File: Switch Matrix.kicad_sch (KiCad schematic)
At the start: 136 parts, among them SW1 RotaryEncoder_Switch, SW10 SW_Push_45deg, SW11 SW_Push_45deg, SW11(2)1 SW_Push_45deg, SW12 SW_Push_45deg, SW13 SW_Push_45deg, SW14 SW_Push_45deg, SW15 SW_Push_45deg, SW16 SW_Push_45deg, SW17 SW_Push_45deg, SW18 SW_Push_45deg, SW19 SW_Push_45deg, SW2 SW_Push_45deg, SW20 SW_Push_45deg, SW21 SW_Push_45deg, SW22 SW_Push_45deg, SW22(1.5)1 SW_Push_45deg, SW23 SW_Push_45deg, SW23(1.5)1 SW_Push_45deg, SW24 SW_Push_45deg, SW24(2)1 SW_Push_45deg, SW24(ISO)1 SW_Push_45deg, SW25(1.25)1 SW_Push_45deg, SW25(1.5)1 SW_Push_45deg, SW25(ortho)1 SW_Push_45deg, SW26 SW_Push_45deg, SW26(ortho)1 SW_Push_45deg, SW27 SW_Push_45deg, SW27(ortho)1 SW_Push_45deg, SW28 SW_Push_45deg, SW28(ortho)1 SW_Push_45deg, SW29 SW_Push_45deg, SW29(ortho)1 SW_Push_45deg, SW3 SW_Push_45deg, SW30 SW_Push_45deg, SW30(ortho)1 SW_Push_45deg, SW31 SW_Push_45deg, SW31(ortho)1 SW_Push_45deg, SW32 SW_Push_45deg, SW32(ortho)1 SW_Push_45deg, SW33 SW_Push_45deg, SW33(ortho)1 SW_Push_45deg, SW34 SW_Push_45deg, SW34(ortho)1 SW_Push_45deg, SW35 SW_Push_45deg, SW35(ortho)1 SW_Push_45deg, SW36(1.25)1 SW_Push_45deg, SW36(1.5)1 SW_Push_45deg, SW36(ortho)1 SW_Push_45deg, SW37 SW_Push_45deg, SW37(1.5)1 SW_Push_45deg, SW38 SW_Push_45deg, SW38(3)1 SW_Push_45deg, SW39 SW_Push_45deg, SW39(1.5)1 SW_Push_45deg, SW4 SW_Push_45deg, SW40(1.25)1 SW_Push_45deg, SW40(1.5)1 SW_Push_45deg, SW40(3)1 SW_Push_45deg, SW41 SW_Push_45deg, SW41(1.75)1 SW_Push_45deg, SW41(1.75a)1 SW_Push_45deg, SW41(1.75a)2 SW_Push_45deg, SW41(2)1 SW_Push_45deg, SW41(2.25)1 SW_Push_45deg, SW42 SW_Push_45deg, SW42(3)1 SW_Push_45deg, SW42(6)1 SW_Push_45deg, SW43 SW_Push_45deg, SW43(1.75)1 SW_Push_45deg, SW43(2)1 SW_Push_45deg, SW43(2.25)1 SW_Push_45deg, SW44 SW_Push_45deg, SW44(1.25)1 SW_Push_45deg, SW44(1.5)1 SW_Push_45deg, SW44(3)1 SW_Push_45deg, SW45 SW_Push_45deg, SW45(1.5)1 SW_Push_45deg, SW46 SW_Push_45deg, SW46(3)1 SW_Push_45deg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

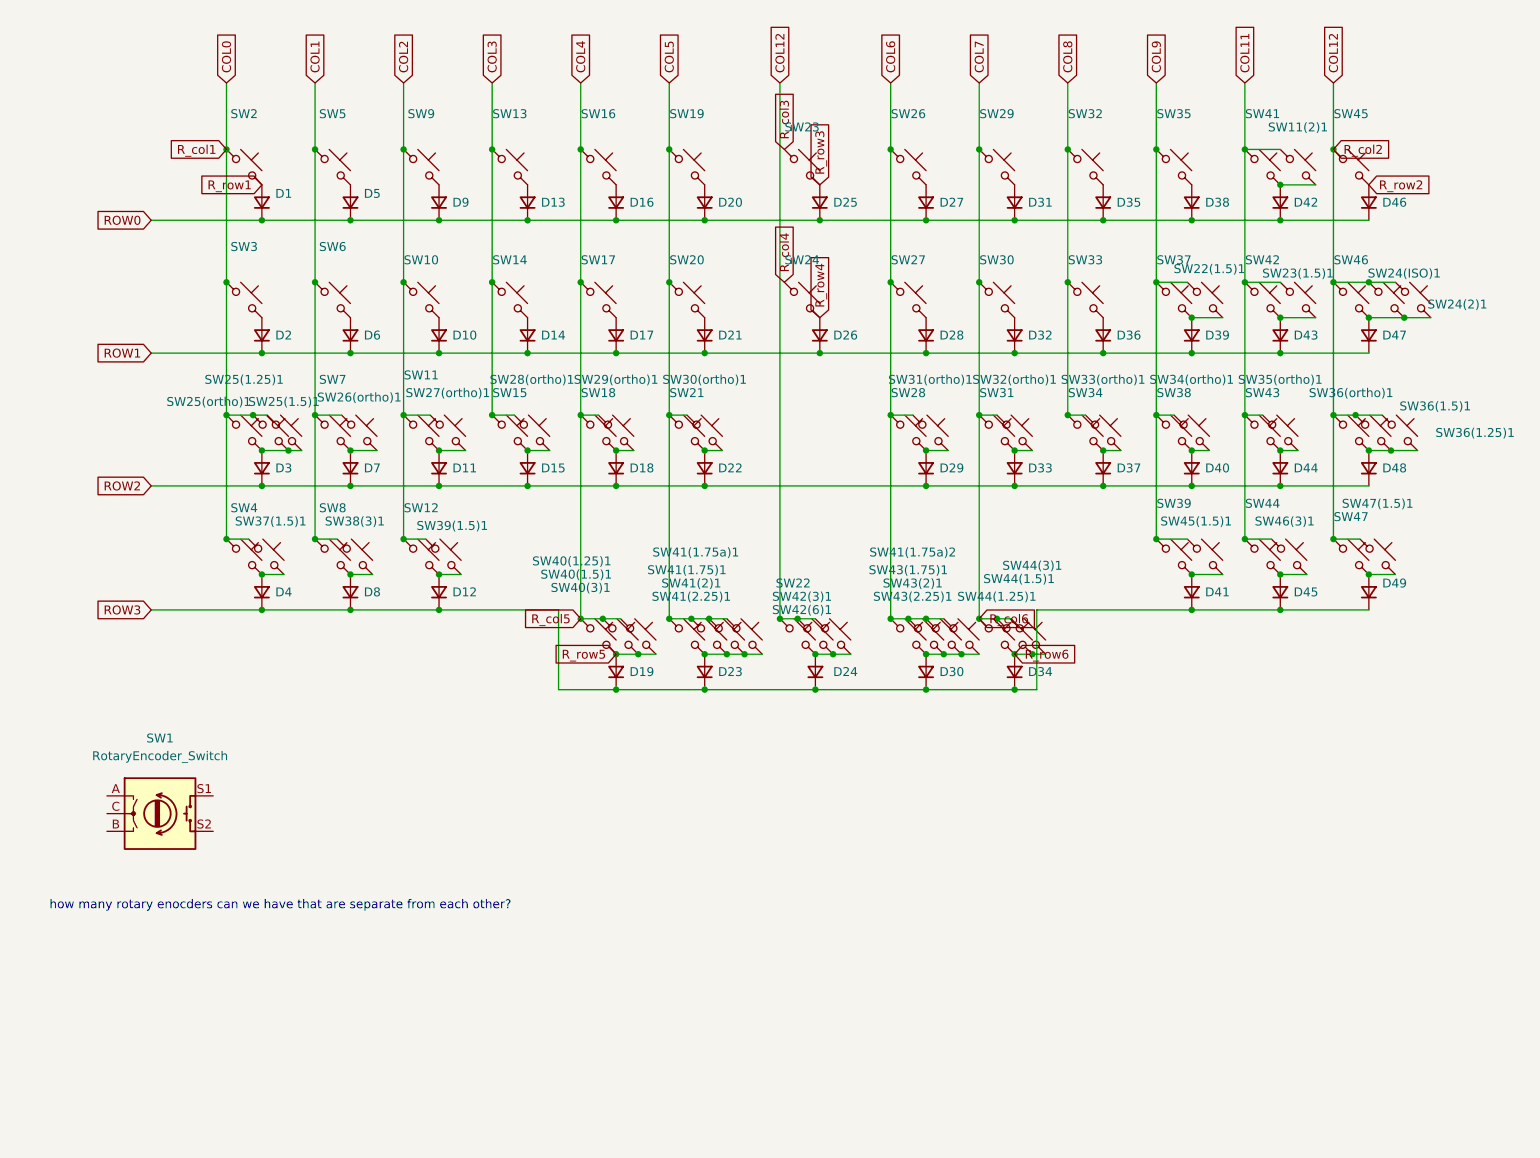
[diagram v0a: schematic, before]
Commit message: edited schematics, assigned footprints
4u spacebar missing, no appropriate footprint in library yet
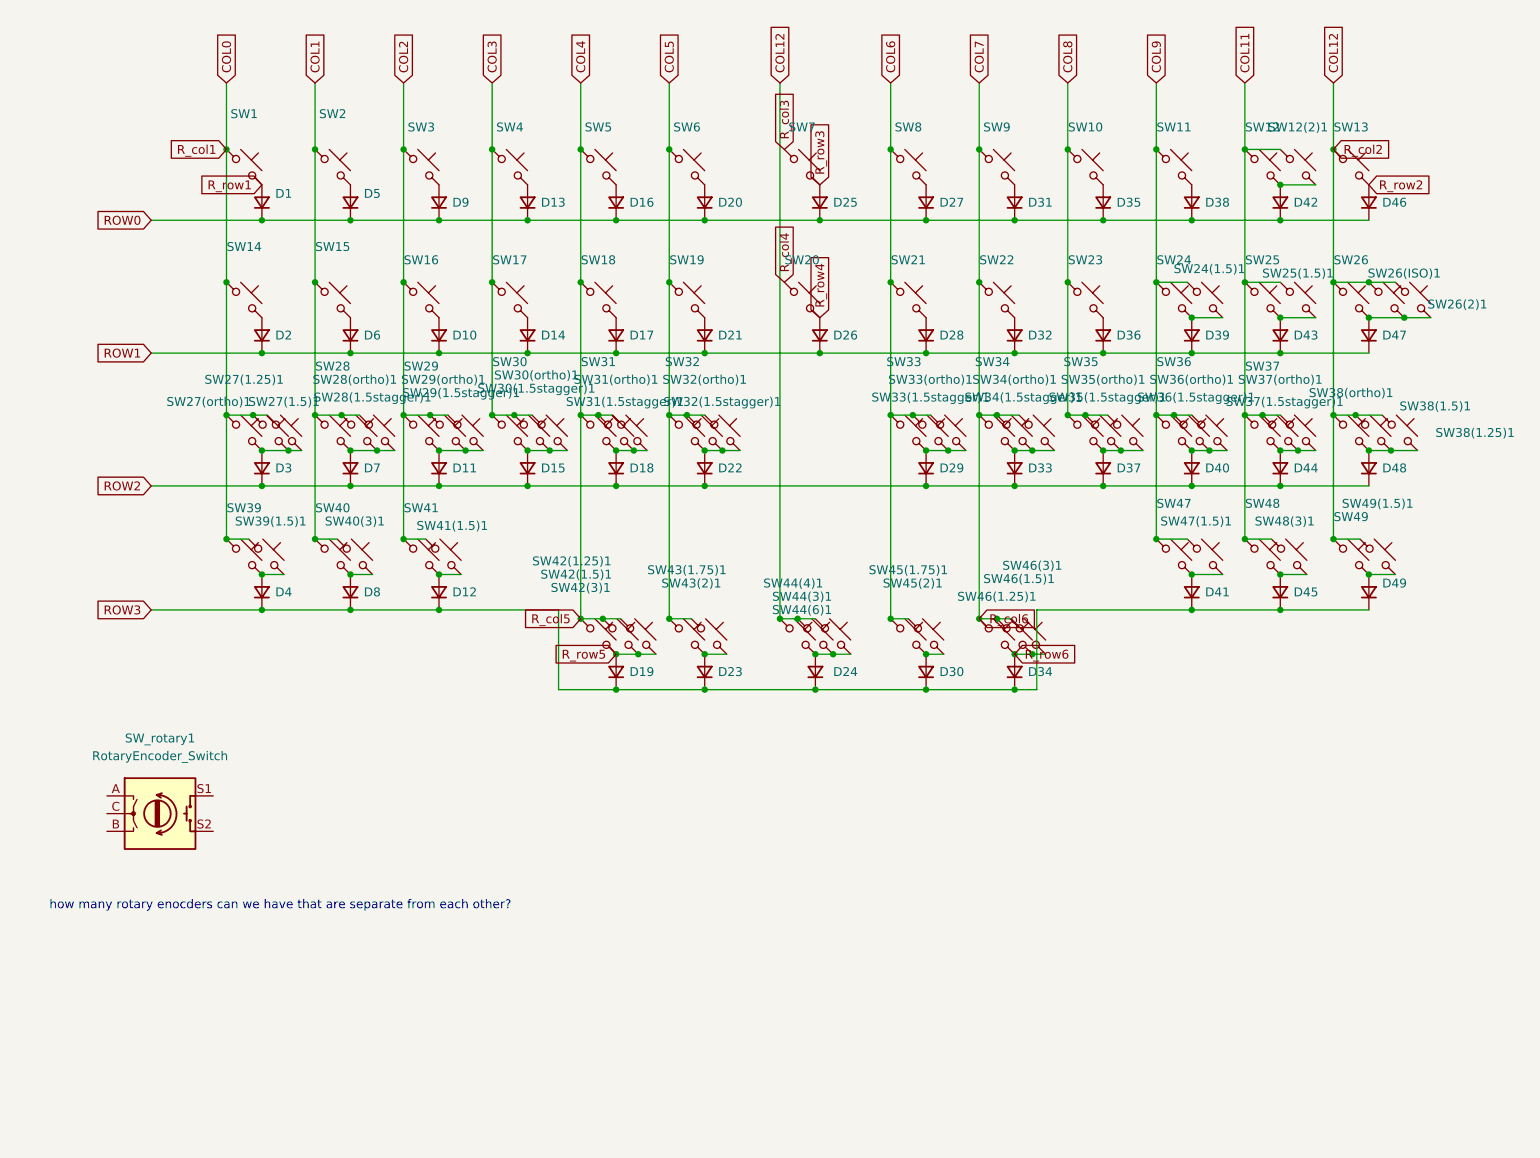
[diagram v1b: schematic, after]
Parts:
- removed SW41(1.75a)1, SW41(1.75a)2, SW41(2.25)1, SW43(2.25)1: SW_Push_45deg, symbol Switch:SW_Push_45deg
- added SW28(1.5stagger)1, SW29(1.5stagger)1, SW30(1.5stagger)1, SW31(1.5stagger)1, SW32(1.5stagger)1, SW33(1.5stagger)1, SW34(1.5stagger)1, SW35(1.5stagger)1, SW36(1.5stagger)1, SW37(1.5stagger)1: SW_Push_45deg, MX_Only:MXOnly-1U-NoLED, symbol Switch:SW_Push_45deg
- D1, D10, D11, D12, D13, D14, D15, D16, D17, D18, D19, D2, D20, D21, D22, D23, D24, D25, D26, D27, D28, D29, D3, D30, D31, D32, D33, D34, D35, D36, D37, D38, D39, D4, D40, D41, D42, D43, D44, D45, D46, D47, D48, D49, D5, D6, D7, D8, D9: footprint (none) -> Diode_SMD:D_SOD-123F
- SW1: renamed from SW2; footprint (none) -> MX_Only:MXOnly-1U-NoLED
- SW10: renamed from SW32; footprint (none) -> MX_Only:MXOnly-1U-NoLED
- SW11: renamed from SW35; footprint (none) -> MX_Only:MXOnly-1U-NoLED
- SW12: renamed from SW41; footprint (none) -> MX_Only:MXOnly-1U-NoLED
- SW12(2)1: renamed from SW11(2)1; footprint (none) -> MX_Only:MXOnly-2U-NoLED
- SW13: renamed from SW45; footprint (none) -> MX_Only:MXOnly-1U-NoLED
- SW14: renamed from SW3; footprint (none) -> MX_Only:MXOnly-1U-NoLED
- SW15: renamed from SW6; footprint (none) -> MX_Only:MXOnly-1U-NoLED
- SW16: renamed from SW10; footprint (none) -> MX_Only:MXOnly-1U-NoLED
- SW17: renamed from SW14; footprint (none) -> MX_Only:MXOnly-1U-NoLED
- SW18: renamed from SW17; footprint (none) -> MX_Only:MXOnly-1U-NoLED
- SW19: renamed from SW20; footprint (none) -> MX_Only:MXOnly-1U-NoLED
- SW2: renamed from SW5; footprint (none) -> MX_Only:MXOnly-1U-NoLED
- SW20: renamed from SW24; footprint (none) -> MX_Only:MXOnly-1U-NoLED
- SW21: renamed from SW27; footprint (none) -> MX_Only:MXOnly-1U-NoLED
- SW22: renamed from SW30; footprint (none) -> MX_Only:MXOnly-1U-NoLED
- SW23: renamed from SW33; footprint (none) -> MX_Only:MXOnly-1U-NoLED
- SW24: renamed from SW37; footprint (none) -> MX_Only:MXOnly-1U-NoLED
- SW24(1.5)1: renamed from SW22(1.5)1; footprint (none) -> MX_Only:MXOnly-1.5U-NoLED
- SW25: renamed from SW42; footprint (none) -> MX_Only:MXOnly-1U-NoLED
- SW25(1.5)1: renamed from SW23(1.5)1; footprint (none) -> MX_Only:MXOnly-1.5U-NoLED
- SW26: renamed from SW46; footprint (none) -> MX_Only:MXOnly-1U-NoLED
- SW26(2)1: renamed from SW24(2)1; footprint (none) -> MX_Only:MXOnly-2U-NoLED
- SW26(ISO)1: renamed from SW24(ISO)1; footprint (none) -> MX_Only:MXOnly-ISO-NoLED
- SW27(1.25)1: renamed from SW25(1.25)1; footprint (none) -> MX_Only:MXOnly-1.25U-NoLED
- SW27(1.5)1: renamed from SW25(1.5)1; footprint (none) -> MX_Only:MXOnly-1.5U-NoLED
- SW27(ortho)1: renamed from SW25(ortho)1; footprint (none) -> MX_Only:MXOnly-1U-NoLED
- SW28: renamed from SW7; footprint (none) -> MX_Only:MXOnly-1U-NoLED
- SW28(ortho)1: renamed from SW26(ortho)1; footprint (none) -> MX_Only:MXOnly-1U-NoLED
- SW29: renamed from SW11; footprint (none) -> MX_Only:MXOnly-1U-NoLED
- SW29(ortho)1: renamed from SW27(ortho)1; footprint (none) -> MX_Only:MXOnly-1U-NoLED
- SW3: renamed from SW9; footprint (none) -> MX_Only:MXOnly-1U-NoLED
- SW30: renamed from SW15; footprint (none) -> MX_Only:MXOnly-1U-NoLED
- SW30(ortho)1: renamed from SW28(ortho)1; footprint (none) -> MX_Only:MXOnly-1U-NoLED
- SW31: renamed from SW18; footprint (none) -> MX_Only:MXOnly-1U-NoLED
- SW31(ortho)1: renamed from SW29(ortho)1; footprint (none) -> MX_Only:MXOnly-1U-NoLED
- SW32: renamed from SW21; footprint (none) -> MX_Only:MXOnly-1U-NoLED
- SW32(ortho)1: renamed from SW30(ortho)1; footprint (none) -> MX_Only:MXOnly-1U-NoLED
- SW33: renamed from SW28; footprint (none) -> MX_Only:MXOnly-1U-NoLED
- SW33(ortho)1: renamed from SW31(ortho)1; footprint (none) -> MX_Only:MXOnly-1U-NoLED
- SW34: renamed from SW31; footprint (none) -> MX_Only:MXOnly-1U-NoLED
- SW34(ortho)1: renamed from SW32(ortho)1; footprint (none) -> MX_Only:MXOnly-1U-NoLED
- SW35: renamed from SW34; footprint (none) -> MX_Only:MXOnly-1U-NoLED
- SW35(ortho)1: renamed from SW33(ortho)1; footprint (none) -> MX_Only:MXOnly-1U-NoLED
- SW36: renamed from SW38; footprint (none) -> MX_Only:MXOnly-1U-NoLED
- SW36(ortho)1: renamed from SW34(ortho)1; footprint (none) -> MX_Only:MXOnly-1U-NoLED
- SW37: renamed from SW43; footprint (none) -> MX_Only:MXOnly-1U-NoLED
- SW37(ortho)1: renamed from SW35(ortho)1; footprint (none) -> MX_Only:MXOnly-1U-NoLED
- SW38(1.25)1: renamed from SW36(1.25)1; footprint (none) -> MX_Only:MXOnly-1.25U-NoLED
- SW38(1.5)1: renamed from SW36(1.5)1; footprint (none) -> MX_Only:MXOnly-1.5U-NoLED
- SW38(ortho)1: renamed from SW36(ortho)1; footprint (none) -> MX_Only:MXOnly-1U-NoLED
- SW39: renamed from SW4; footprint (none) -> MX_Only:MXOnly-1U-NoLED
- SW39(1.5)1: renamed from SW37(1.5)1; footprint (none) -> MX_Only:MXOnly-1.5U-NoLED
- SW4: renamed from SW13; footprint (none) -> MX_Only:MXOnly-1U-NoLED
- SW40: renamed from SW8; footprint (none) -> MX_Only:MXOnly-1U-NoLED
- SW40(3)1: renamed from SW38(3)1; footprint (none) -> MX_Only:MXOnly-3U-ReversedStabilizers-NoLED
- SW41: renamed from SW12; footprint (none) -> MX_Only:MXOnly-1U-NoLED
- SW41(1.5)1: renamed from SW39(1.5)1; footprint (none) -> MX_Only:MXOnly-1.5U-NoLED
- SW42(1.25)1: renamed from SW40(1.25)1; footprint (none) -> MX_Only:MXOnly-1.25U-NoLED
- SW42(1.5)1: renamed from SW40(1.5)1; footprint (none) -> MX_Only:MXOnly-1.5U-NoLED
- SW42(3)1: renamed from SW40(3)1; footprint (none) -> MX_Only:MXOnly-3U-ReversedStabilizers-NoLED
- SW43(1.75)1: renamed from SW41(1.75)1; footprint (none) -> MX_Only:MXOnly-1.75U-NoLED
- SW43(2)1: renamed from SW41(2)1; footprint (none) -> MX_Only:MXOnly-2U-ReversedStabilizers-NoLED
- SW44(3)1: renamed from SW42(3)1; footprint (none) -> MX_Only:MXOnly-3U-ReversedStabilizers-NoLED
- SW44(6)1: renamed from SW42(6)1; footprint (none) -> MX_Only:MXOnly-6U-Centered-ReversedStabilizers-NoLED
- SW45(1.75)1: renamed from SW43(1.75)1; footprint (none) -> MX_Only:MXOnly-1.75U-NoLED
- SW45(2)1: renamed from SW43(2)1; footprint (none) -> MX_Only:MXOnly-2U-ReversedStabilizers-NoLED
- SW46(1.25)1: renamed from SW44(1.25)1; footprint (none) -> MX_Only:MXOnly-1.25U-NoLED
- SW46(1.5)1: renamed from SW44(1.5)1; footprint (none) -> MX_Only:MXOnly-1.5U-NoLED
- SW46(3)1: renamed from SW44(3)1; footprint (none) -> MX_Only:MXOnly-3U-ReversedStabilizers-NoLED
- SW47: renamed from SW39; footprint (none) -> MX_Only:MXOnly-1U-NoLED
- SW47(1.5)1: renamed from SW45(1.5)1; footprint (none) -> MX_Only:MXOnly-1.5U-NoLED
- SW48: renamed from SW44; footprint (none) -> MX_Only:MXOnly-1U-NoLED
- SW48(3)1: renamed from SW46(3)1; footprint (none) -> MX_Only:MXOnly-3U-ReversedStabilizers-NoLED
- SW49: renamed from SW47; footprint (none) -> MX_Only:MXOnly-1U-NoLED
- SW49(1.5)1: renamed from SW47(1.5)1; footprint (none) -> MX_Only:MXOnly-1.5U-NoLED
- SW5: renamed from SW16; footprint (none) -> MX_Only:MXOnly-1U-NoLED
- SW6: renamed from SW19; footprint (none) -> MX_Only:MXOnly-1U-NoLED
- SW7: renamed from SW23; footprint (none) -> MX_Only:MXOnly-1U-NoLED
- SW8: renamed from SW26; footprint (none) -> MX_Only:MXOnly-1U-NoLED
- SW9: renamed from SW29; footprint (none) -> MX_Only:MXOnly-1U-NoLED
- SW_rotary1: renamed from SW1; footprint (none) -> Keebio-Parts:RotaryEncoder_EC11-no-legs
- renumbered SW22 to SW44(4)1
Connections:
- net COL1: now also SW28(1.5stagger)1.1
- net COL11: now also SW37(1.5stagger)1.1
- net COL2: now also SW29(1.5stagger)1.1
- net COL3: now also SW30(1.5stagger)1.1
- net COL4: now also SW31(1.5stagger)1.1
- net COL5: now also SW32(1.5stagger)1.1
- net COL6: now also SW33(1.5stagger)1.1
- net COL7: now also SW34(1.5stagger)1.1
- net COL8: now also SW35(1.5stagger)1.1
- net COL9: now also SW36(1.5stagger)1.1
- net at D29.2 (A), SW33(ortho)1.2, SW33.2: now also SW33(1.5stagger)1.2
- net at D18.2 (A), SW31(ortho)1.2, SW31.2: now also SW31(1.5stagger)1.2
- net at D37.2 (A), SW35(ortho)1.2, SW35.2: now also SW35(1.5stagger)1.2
- net at D7.2 (A), SW28(ortho)1.2, SW28.2: now also SW28(1.5stagger)1.2
- net at D11.2 (A), SW29(ortho)1.2, SW29.2: now also SW29(1.5stagger)1.2
- net at D15.2 (A), SW30(ortho)1.2, SW30.2: now also SW30(1.5stagger)1.2
- net at D40.2 (A), SW36(ortho)1.2, SW36.2: now also SW36(1.5stagger)1.2
- net at D22.2 (A), SW32(ortho)1.2, SW32.2: now also SW32(1.5stagger)1.2
- net at D33.2 (A), SW34(ortho)1.2, SW34.2: now also SW34(1.5stagger)1.2
- net at D44.2 (A), SW37(ortho)1.2, SW37.2: now also SW37(1.5stagger)1.2

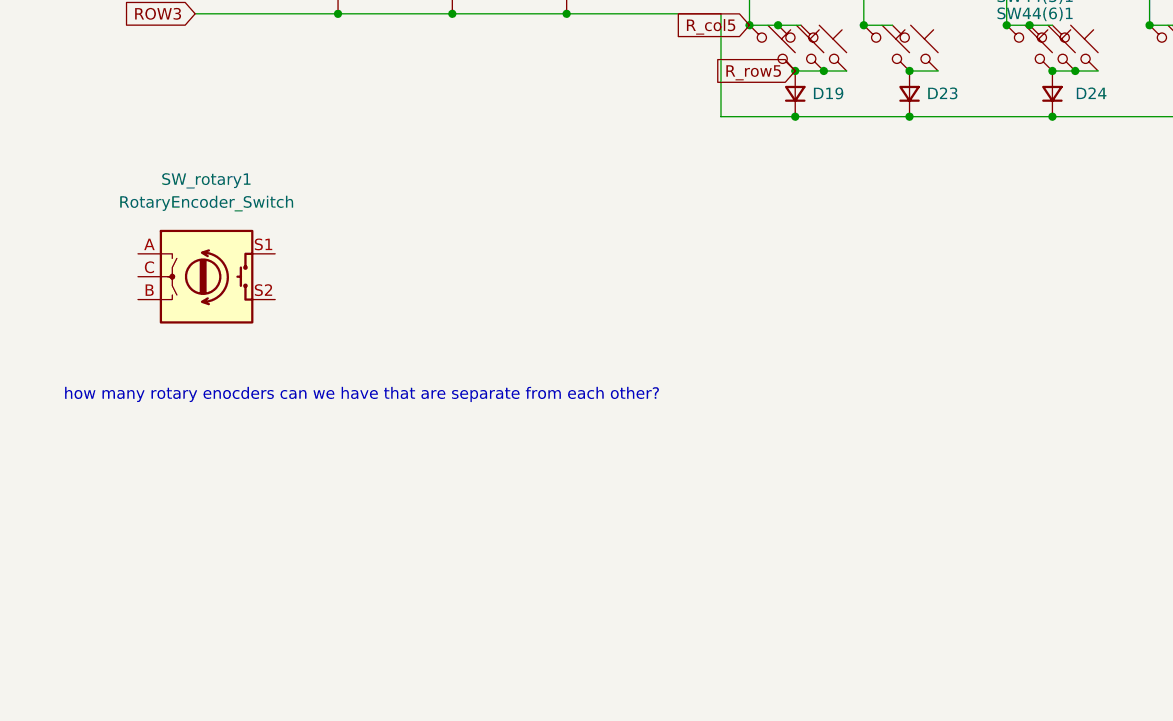
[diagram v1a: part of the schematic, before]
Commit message: arrange footprints
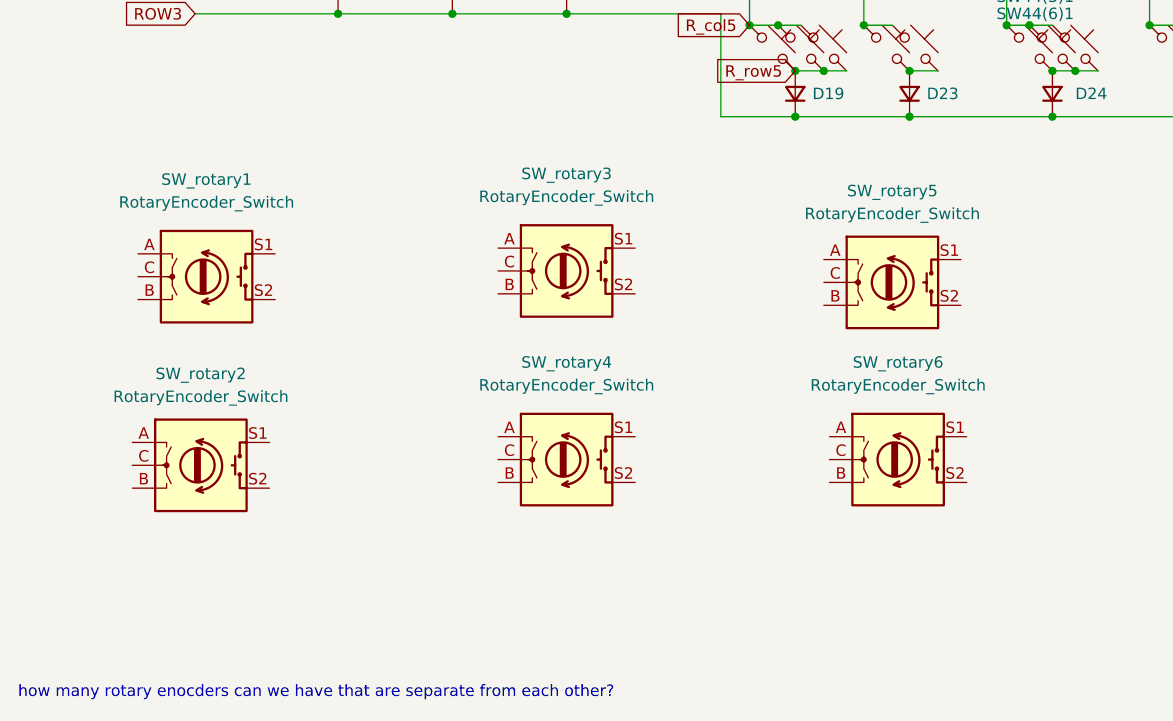
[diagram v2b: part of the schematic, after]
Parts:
- added SW_rotary2, SW_rotary3, SW_rotary4, SW_rotary5, SW_rotary6: RotaryEncoder_Switch, Keebio-Parts:RotaryEncoder_EC11-no-legs, symbol Device:RotaryEncoder_Switch
